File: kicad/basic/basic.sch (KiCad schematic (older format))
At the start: 16 parts, among them P1 CONN_01X15, P2 CONN_01X15, P3 CONN_01X15, P4 CONN_01X15, P5 CONN_01X01, P6 CONN_01X01, P7 CONN_01X01, P8 CONN_01X01

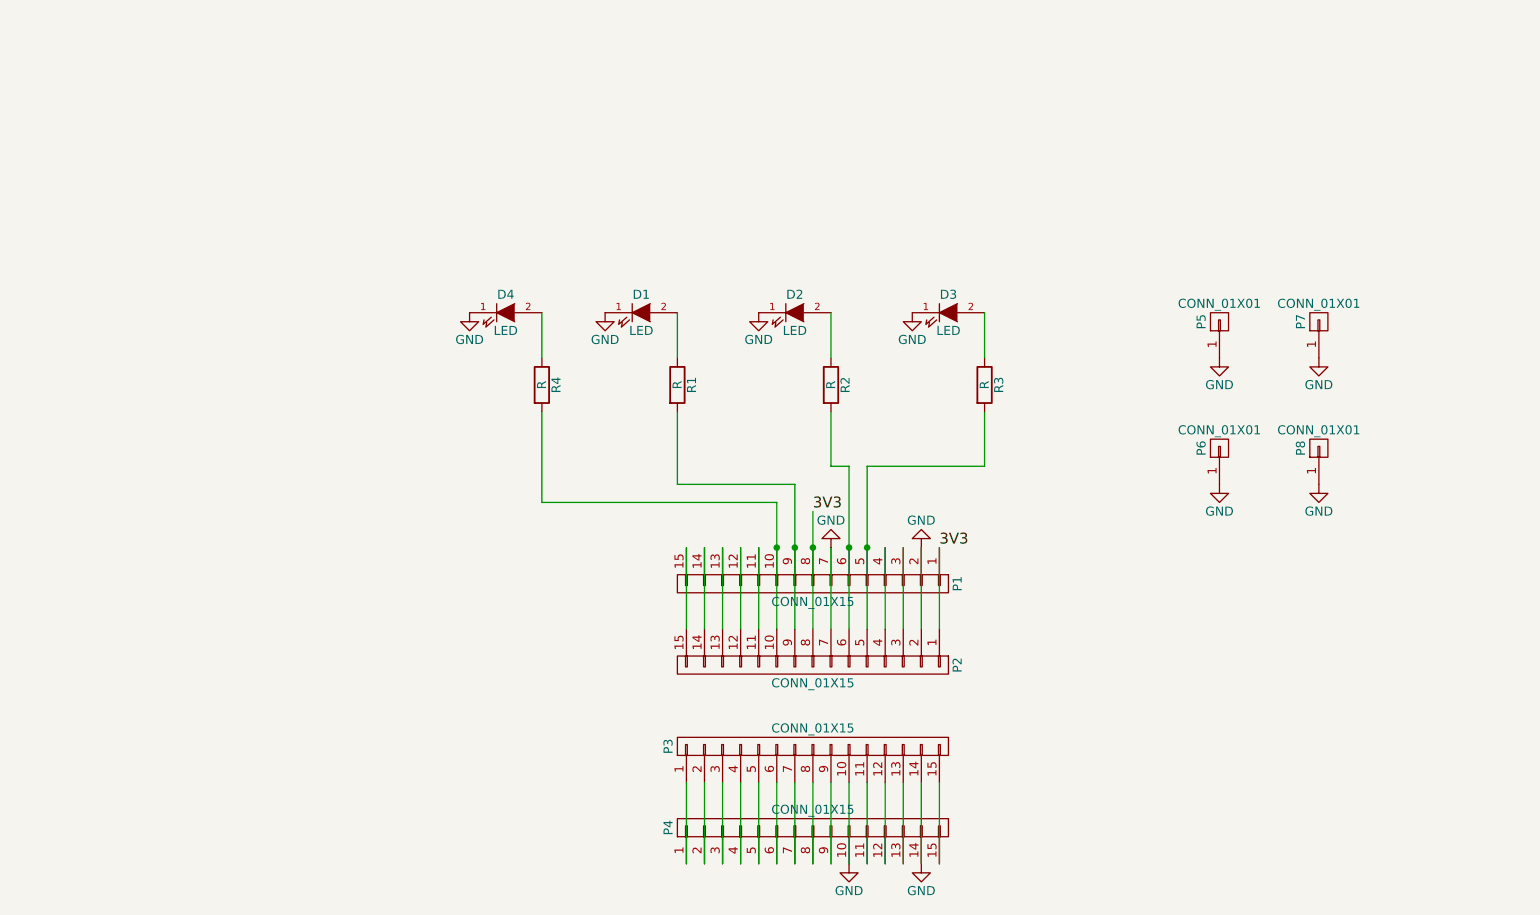
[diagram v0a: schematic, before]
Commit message: Breakout only the GPIO
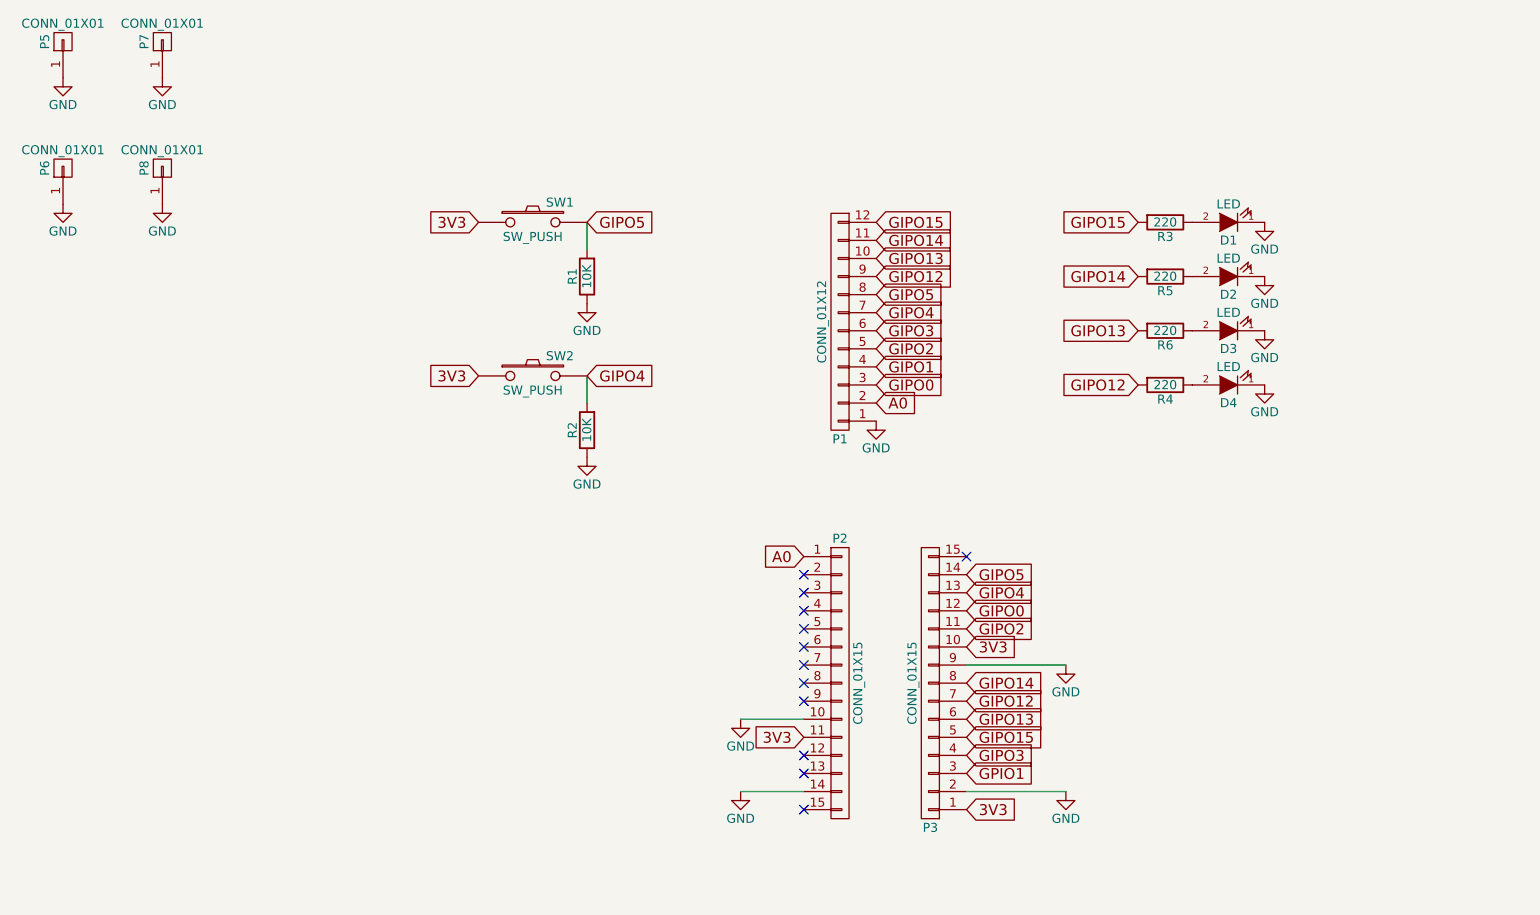
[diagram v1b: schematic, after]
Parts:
- removed P1, P4: CONN_01X15, Socket_Strips:Socket_Strip_Straight_1x15, symbol CONN_01X15
- added P1: CONN_01X12, Socket_Strips:Socket_Strip_Straight_1x12, symbol CONN_01X12
- added R5, R6: 220, Resistors_SMD:R_0805_HandSoldering, symbol R
- added SW1, SW2: SW_PUSH, Buttons_Switches_ThroughHole:SW_PUSH_SMALL, symbol SW_PUSH
- R1, R2: value R -> 10K
- R3, R4: value R -> 220
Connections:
- net 3V3: now also P2.11 (P11), P3.1 (P1), P3.10 (P10), SW1.1, SW2.1; no longer P2.1 (P1), P2.8 (P8)
- net GND: now also P2.10 (P10), P2.14 (P14), P3.2 (P2), P3.9 (P9), R1.1, R2.1, P1.1 (P1); no longer P2.2 (P2), P2.7 (P7), P3.10 (P10), P3.14 (P14)
- net at D1.2 (A): now also R3.1; no longer R1.1
- net at D2.2 (A): now also R5.1; no longer R2.1
- net at D3.2 (A): now also R6.1; no longer R3.1
- net at P2.9 (P9): no longer R1.2
- net at P2.6 (P6): no longer R2.2
- net at P2.5 (P5): no longer R3.2
- net GIPO12: now reaches R4.2
- net GIPO12: now also P3.7 (P7), P1.9 (P9); no longer P2.10 (P10)
- net GIPO2: now reaches P3.11 (P11)
- net GIPO2: now also P1.5 (P5)
- net GIPO0: now reaches P3.12 (P12)
- net GIPO0: now also P1.3 (P3)
- net GIPO4: now reaches P3.13 (P13)
- net GIPO4: now also R2.2, P1.7 (P7), SW2.2
- net GPIO1: now reaches P3.3 (P3)
- net GIPO3: now reaches P3.4 (P4)
- net GIPO3: now also P1.6 (P6)
- net GIPO15: now reaches P3.5 (P5)
- net GIPO15: now also R3.2, P1.12 (P12)
- net GIPO13: now reaches P3.6 (P6)
- net GIPO13: now also P1.10 (P10), R6.2
- net GIPO14: now reaches P3.8 (P8)
- net GIPO14: now also P1.11 (P11), R5.2
- new net A0: P1.2 (P2), P2.1 (P1)
- new net GIPO1: P1.4 (P4)
- new net GIPO5: P1.8 (P8), P3.14 (P14), R1.2, SW1.2
- no-connect marks 0 -> 12
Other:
- moved on the sheet: D4, P5, P6, P7, P8, R4

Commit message: Through hole parts
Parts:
- removed P1: CONN_01X12, Socket_Strips:Socket_Strip_Straight_1x12, symbol CONN_01X12
- added P4, P9: CONN_01X06, Socket_Strips:Socket_Strip_Straight_1x06, symbol CONN_01X06
- R1, R2, R3, R4, R5, R6: footprint Resistors_SMD:R_0805_HandSoldering -> Resistors_ThroughHole:Resistor_Horizontal_RM10mm
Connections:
- net A0: now also P4.2 (P2)
- net GIPO1: now also P4.3 (P3)
- net GIPO12: now also P9.3 (P3)
- net GIPO13: now also P9.4 (P4)
- net GIPO14: now also P9.5 (P5)
- net GIPO15: now also P9.6 (P6)
- net GIPO2: now also P4.4 (P4)
- net GIPO3: now also P4.5 (P5)
- net GIPO4: now also P4.6 (P6)
- net GIPO5: now also P9.2 (P2)
- net GND: now also P4.1 (P1), P9.1 (P1)
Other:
- moved on the sheet: D1, D2, D3, D4, R1, R2, R3, R4, R5, R6, SW1, SW2

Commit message: Routing
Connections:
- net GIPO1 is gone; now on net D3: P4.3 (P3)
- net 3V3: now also P2.5 (P5); no longer P2.11 (P11), P3.10 (P10)
- net A0: now also P2.15 (P15), P4.6 (P6); no longer P2.1 (P1), P4.2 (P2)
- net GND: now also P2.2 (P2), P2.6 (P6); no longer P2.10 (P10), P2.14 (P14)
- net GIPO0 renamed D3
- removed net GIPO12: P3.7 (P7), P9.3 (P3), R4.2
- removed net GIPO13: P3.6 (P6), P9.4 (P4), R6.2
- removed net GIPO14: P3.8 (P8), P9.5 (P5), R5.2
- removed net GIPO15: P3.5 (P5), P9.6 (P6), R3.2
- net GIPO2 renamed D2
- net D2: now also P3.13 (P13), R2.2, SW2.2; no longer P3.11 (P11)
- net GIPO3 renamed D1
- net D1: now also P3.14 (P14), R1.2, SW1.2; no longer P3.4 (P4)
- removed net GIPO4: P3.13 (P13), P4.6 (P6), R2.2, SW2.2
- removed net GIPO5: P3.14 (P14), P9.2 (P2), R1.2, SW1.2
- net GPIO1 renamed D10
- net D10: now also P9.2 (P2), R4.2
- new net D4: P3.11 (P11), P4.2 (P2)
- new net D6: P3.7 (P7), P9.6 (P6)
- new net D7: P3.6 (P6), P9.5 (P5), R3.2
- new net D8: P3.5 (P5), P9.4 (P4), R5.2
- new net D9: P3.4 (P4), P9.3 (P3), R6.2
- no-connect marks 12 -> 14
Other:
- moved on the sheet: P2, P3
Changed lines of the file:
@@
 	1    0    0    -1
 $EndComp
-Text GLabel 5500 2700 0    60   Input ~ 0
-GIPO1
-Text GLabel 5500 2500 0    60   Input ~ 0
-GIPO3
-Text GLabel 6400 2400 2    60   Input ~ 0
-GIPO15
-Text GLabel 6400 2600 2    60   Input ~ 0
-GIPO13
-Text GLabel 6400 2700 2    60   Input ~ 0
-GIPO12
-Text GLabel 6400 2500 2    60   Input ~ 0
-GIPO14
-Text GLabel 5500 2600 0    60   Input ~ 0
-GIPO2
-Text GLabel 5500 2400 0    60   Input ~ 0
-GIPO4
-Text GLabel 6400 2800 2    60   Input ~ 0
-GIPO5
 $Comp
 L LED D3
@@
 	1    0    0    -1
 $EndComp
-Text GLabel 8550 2300 0    60   Input ~ 0
-GIPO15
-Text GLabel 8550 2600 0    60   Input ~ 0
-GIPO14
-Text GLabel 8550 2900 0    60   Input ~ 0
-GIPO13
-Text GLabel 8550 3200 0    60   Input ~ 0
-GIPO12
 $Comp
 L SW_PUSH SW1
@@
 	1    0    0    -1
 $EndComp
-Text GLabel 3850 2200 2    60   Input ~ 0
-GIPO5
-Text GLabel 3850 3050 2    60   Input ~ 0
-GIPO4
 $Comp
 L CONN_01X15 P2
 U 1 1 570F9B9A
-P 5700 4750
-F 0 "P2" H 5700 5550 50  0000 C CNN
-F 1 "CONN_01X15" V 5800 4750 50  0000 C CNN
-F 2 "Socket_Strips:Socket_Strip_Straight_1x15" H 5700 4750 50  0001 C CNN
-F 3 "" H 5700 4750 50  0000 C CNN
-	1    5700 4750
-	1    0    0    -1
+P 5700 4200
+F 0 "P2" H 5700 5000 50  0000 C CNN
+F 1 "CONN_01X15" V 5800 4200 50  0000 C CNN
+F 2 "Socket_Strips:Socket_Strip_Straight_1x15" H 5700 4200 50  0001 C CNN
+F 3 "" H 5700 4200 50  0000 C CNN
+	1    5700 4200
+	1    0    0    1
 $EndComp
 $Comp
 L CONN_01X15 P3
 U 1 1 570F9E13
-P 6200 4750
-F 0 "P3" H 6200 5550 50  0000 C CNN
-F 1 "CONN_01X15" V 6300 4750 50  0000 C CNN
-F 2 "Socket_Strips:Socket_Strip_Straight_1x15" H 6200 4750 50  0001 C CNN
-F 3 "" H 6200 4750 50  0000 C CNN
-	1    6200 4750
+P 6200 4200
+F 0 "P3" H 6200 5000 50  0000 C CNN
+F 1 "CONN_01X15" V 6300 4200 50  0000 C CNN
+F 2 "Socket_Strips:Socket_Strip_Straight_1x15" H 6200 4200 50  0001 C CNN
+F 3 "" H 6200 4200 50  0000 C CNN
+	1    6200 4200
 	-1   0    0    1
 $EndComp
@@
 L GND #PWR09
 U 1 1 570F9FDE
-P 6950 5350
-F 0 "#PWR09" H 6950 5100 50  0001 C CNN
-F 1 "GND" H 6950 5200 50  0000 C CNN
-F 2 "" H 6950 5350 50  0000 C CNN
-F 3 "" H 6950 5350 50  0000 C CNN
-	1    6950 5350
-	1    0    0    -1
-$EndComp
-Text GLabel 6400 5450 2    60   Input ~ 0
+P 6950 4800
+F 0 "#PWR09" H 6950 4550 50  0001 C CNN
+F 1 "GND" H 6950 4650 50  0000 C CNN
+F 2 "" H 6950 4800 50  0000 C CNN
+F 3 "" H 6950 4800 50  0000 C CNN
+	1    6950 4800
+	1    0    0    -1
+$EndComp
+Text GLabel 6400 4900 2    60   Input ~ 0
 3V3
-Text GLabel 5500 5050 0    60   Input ~ 0
-3V3
-Text GLabel 6400 4550 2    60   Input ~ 0
+Text GLabel 5500 4500 0    60   Input ~ 0
 3V3
 $Comp
 L GND #PWR010
 U 1 1 570FA0BF
-P 6950 4650
-F 0 "#PWR010" H 6950 4400 50  0001 C CNN
-F 1 "GND" H 6950 4500 50  0000 C CNN
-F 2 "" H 6950 4650 50  0000 C CNN
-F 3 "" H 6950 4650 50  0000 C CNN
-	1    6950 4650
+P 6950 4100
+F 0 "#PWR010" H 6950 3850 50  0001 C CNN
+F 1 "GND" H 6950 3950 50  0000 C CNN
+F 2 "" H 6950 4100 50  0000 C CNN
+F 3 "" H 6950 4100 50  0000 C CNN
+	1    6950 4100
 	1    0    0    -1
 $EndComp
@@
 L GND #PWR011
 U 1 1 570FA103
-P 5150 5350
-F 0 "#PWR011" H 5150 5100 50  0001 C CNN
-F 1 "GND" H 5150 5200 50  0000 C CNN
-F 2 "" H 5150 5350 50  0000 C CNN
-F 3 "" H 5150 5350 50  0000 C CNN
-	1    5150 5350
+P 5150 4800
+F 0 "#PWR011" H 5150 4550 50  0001 C CNN
+F 1 "GND" H 5150 4650 50  0000 C CNN
+F 2 "" H 5150 4800 50  0000 C CNN
+F 3 "" H 5150 4800 50  0000 C CNN
+	1    5150 4800
 	1    0    0    -1
 $EndComp
@@
 L GND #PWR012
 U 1 1 570FA147
-P 5150 4950
-F 0 "#PWR012" H 5150 4700 50  0001 C CNN
-F 1 "GND" H 5150 4800 50  0000 C CNN
-F 2 "" H 5150 4950 50  0000 C CNN
-F 3 "" H 5150 4950 50  0000 C CNN
-	1    5150 4950
-	1    0    0    -1
-$EndComp
-Text GLabel 5500 4050 0    60   Input ~ 0
+P 5150 4400
+F 0 "#PWR012" H 5150 4150 50  0001 C CNN
+F 1 "GND" H 5150 4250 50  0000 C CNN
+F 2 "" H 5150 4400 50  0000 C CNN
+F 3 "" H 5150 4400 50  0000 C CNN
+	1    5150 4400
+	1    0    0    -1
+$EndComp
+Text GLabel 5500 3500 0    60   Input ~ 0
 A0
-Text GLabel 5500 2800 0    60   Input ~ 0
+Text GLabel 5500 2400 0    60   Input ~ 0
 A0
-Text GLabel 6400 5250 2    60   Input ~ 0
-GPIO1
-Text GLabel 6400 4350 2    60   Input ~ 0
-GIPO0
-Text GLabel 6400 5150 2    60   Input ~ 0
-GIPO3
-Text GLabel 6400 5050 2    60   Input ~ 0
-GIPO15
-Text GLabel 6400 4950 2    60   Input ~ 0
-GIPO13
-Text GLabel 6400 4850 2    60   Input ~ 0
-GIPO12
-Text GLabel 6400 4450 2    60   Input ~ 0
-GIPO2
-Text GLabel 6400 4250 2    60   Input ~ 0
-GIPO4
-Text GLabel 6400 4150 2    60   Input ~ 0
-GIPO5
-Wire Wire Line
-	6400 5350 6950 5350
-Wire Wire Line
-	6400 4650 6950 4650
-Text GLabel 6400 4750 2    60   Input ~ 0
-GIPO14
-NoConn ~ 6400 4050
-NoConn ~ 5500 4150
-NoConn ~ 5500 4250
-NoConn ~ 5500 4350
-NoConn ~ 5500 4450
-NoConn ~ 5500 4550
-NoConn ~ 5500 4650
-NoConn ~ 5500 4750
-NoConn ~ 5500 4850
-NoConn ~ 5500 5150
-NoConn ~ 5500 5250
-NoConn ~ 5500 5450
-Wire Wire Line
-	5150 4950 5500 4950
-Wire Wire Line
-	5150 5350 5500 5350
+Text GLabel 6400 4700 2    60   Input ~ 0
+D10
+Text GLabel 6400 3800 2    60   Input ~ 0
+D3
+Text GLabel 6400 4600 2    60   Input ~ 0
+D9
+Text GLabel 6400 4500 2    60   Input ~ 0
+D8
+Text GLabel 6400 4400 2    60   Input ~ 0
+D7
+Text GLabel 6400 4300 2    60   Input ~ 0
+D6
+Text GLabel 6400 3900 2    60   Input ~ 0
+D4
+Text GLabel 6400 3700 2    60   Input ~ 0
+D2
+Text GLabel 6400 3600 2    60   Input ~ 0
+D1
+Wire Wire Line
+	6400 4800 6950 4800
+Wire Wire Line
+	6400 4100 6950 4100
+NoConn ~ 6400 3500
+NoConn ~ 5500 3600
+NoConn ~ 5500 3700
+NoConn ~ 5500 3800
+NoConn ~ 5500 3900
+NoConn ~ 5500 4000
+NoConn ~ 5500 4100
+NoConn ~ 5500 4200
+NoConn ~ 5500 4300
+NoConn ~ 5500 4600
+NoConn ~ 5500 4700
+NoConn ~ 5500 4900
+Wire Wire Line
+	5150 4400 5500 4400
+Wire Wire Line
+	5150 4800 5500 4800
 $Comp
 L R R1
@@
 	1    0    0    -1
 $EndComp
+Text GLabel 6400 2800 2    60   Input ~ 0
+D10
+Text GLabel 6400 2700 2    60   Input ~ 0
+D9
+Text GLabel 6400 2600 2    60   Input ~ 0
+D8
+Text GLabel 6400 2500 2    60   Input ~ 0
+D7
+Text GLabel 6400 2400 2    60   Input ~ 0
+D6
+Text GLabel 5500 2500 0    60   Input ~ 0
+D1
+Text GLabel 5500 2600 0    60   Input ~ 0
+D2
+Text GLabel 5500 2700 0    60   Input ~ 0
+D3
+Text GLabel 5500 2800 0    60   Input ~ 0
+D4
+NoConn ~ 6400 4200
+Text GLabel 8550 3200 0    60   Input ~ 0
+D10
+Text GLabel 8550 2900 0    60   Input ~ 0
+D9
+Text GLabel 8550 2600 0    60   Input ~ 0
+D8
+Text GLabel 8550 2300 0    60   Input ~ 0
+D7
+Text GLabel 3850 2200 2    60   Input ~ 0
+D1
+Text GLabel 3850 3050 2    60   Input ~ 0
+D2
+NoConn ~ 6400 4000
 $EndSCHEMATC
